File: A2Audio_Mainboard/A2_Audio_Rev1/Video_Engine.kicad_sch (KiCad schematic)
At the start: 21 parts, among them U18 LT6711A, U20 AP2112K-1.8, U22 AP2112K-1.2, Y2 27MHz

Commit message: Added footprints and a few more parts.
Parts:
- C58, C59, C60, C61, C62, C63, C72, C73, C74, C75, C76, C77, C78, C79, C80, C81: footprint (none) -> Capacitor_SMD:C_0402_1005Metric
- R26: footprint (none) -> Resistor_SMD:R_0402_1005Metric
- Y2: footprint (none) -> Crystal:Crystal_SMD_3225-4Pin_3.2x2.5mm
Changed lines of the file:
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@@
 			)
 		)
-		(property "Footprint" ""
+		(property "Footprint" "Capacitor_SMD:C_0402_1005Metric"
 			(at 198.12 114.6048 0)
 			(hide yes)
@@
 			)
 		)
-		(property "Footprint" ""
+		(property "Footprint" "Capacitor_SMD:C_0402_1005Metric"
 			(at 198.12 79.0448 0)
 			(hide yes)
@@
 			)
 		)
-		(property "Footprint" ""
+		(property "Footprint" "Capacitor_SMD:C_0402_1005Metric"
 			(at 198.12 131.1148 0)
 			(hide yes)
@@
 			)
 		)
-		(property "Footprint" ""
+		(property "Footprint" "Resistor_SMD:R_0402_1005Metric"
 			(at 77.47 114.808 90)
 			(hide yes)
@@
 			)
 		)
-		(property "Footprint" ""
+		(property "Footprint" "Crystal:Crystal_SMD_3225-4Pin_3.2x2.5mm"
 			(at 62.23 82.55 0)
 			(hide yes)
@@
 			)
 		)
-		(property "Footprint" ""
+		(property "Footprint" "Capacitor_SMD:C_0402_1005Metric"
 			(at 523.5448 66.04 0)
 			(hide yes)
@@
 			)
 		)
-		(property "Footprint" ""
+		(property "Footprint" "Capacitor_SMD:C_0402_1005Metric"
 			(at 198.12 71.4248 0)
 			(hide yes)
@@
 			)
 		)
-		(property "Footprint" ""
+		(property "Footprint" "Capacitor_SMD:C_0402_1005Metric"
 			(at 475.2848 62.23 0)
 			(hide yes)
@@
 			)
 		)
-		(property "Footprint" ""
+		(property "Footprint" "Capacitor_SMD:C_0402_1005Metric"
 			(at 198.12 104.4448 0)
 			(hide yes)
@@
 			)
 		)
-		(property "Footprint" ""
+		(property "Footprint" "Capacitor_SMD:C_0402_1005Metric"
 			(at 72.39 104.4448 0)
 			(hide yes)
@@
 			)
 		)
-		(property "Footprint" ""
+		(property "Footprint" "Capacitor_SMD:C_0402_1005Metric"
 			(at 198.12 95.5548 0)
 			(hide yes)
@@
 			)
 		)
-		(property "Footprint" ""
+		(property "Footprint" "Capacitor_SMD:C_0402_1005Metric"
 			(at 72.39 99.3648 0)
 			(hide yes)
@@
 			)
 		)
-		(property "Footprint" ""
+		(property "Footprint" "Capacitor_SMD:C_0402_1005Metric"
 			(at 198.12 87.9348 0)
 			(hide yes)
@@
 			)
 		)
-		(property "Footprint" ""
+		(property "Footprint" "Capacitor_SMD:C_0402_1005Metric"
 			(at 439.42 53.0352 0)
 			(hide yes)
@@
 			)
 		)
-		(property "Footprint" ""
+		(property "Footprint" "Capacitor_SMD:C_0402_1005Metric"
 			(at 41.6052 82.55 0)
 			(hide yes)
@@
 			)
 		)
-		(property "Footprint" ""
+		(property "Footprint" "Capacitor_SMD:C_0402_1005Metric"
 			(at 468.9348 85.09 0)
 			(hide yes)
@@
 			)
 		)
-		(property "Footprint" ""
+		(property "Footprint" "Capacitor_SMD:C_0402_1005Metric"
 			(at 27.6352 82.55 0)
 			(hide yes)
@@
 			)
 		)
-		(property "Footprint" ""
+		(property "Footprint" "Capacitor_SMD:C_0402_1005Metric"
 			(at 198.12 123.4948 0)
 			(hide yes)

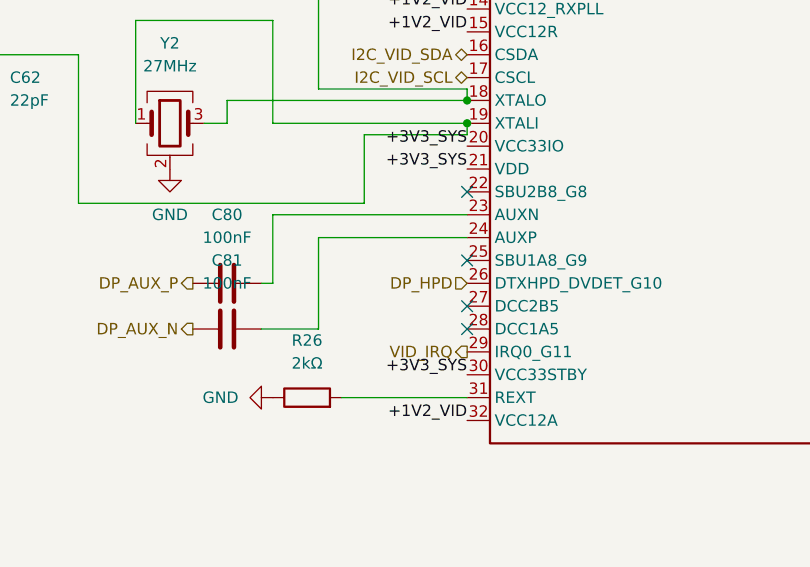
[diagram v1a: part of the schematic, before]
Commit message: Fixing ERC errors
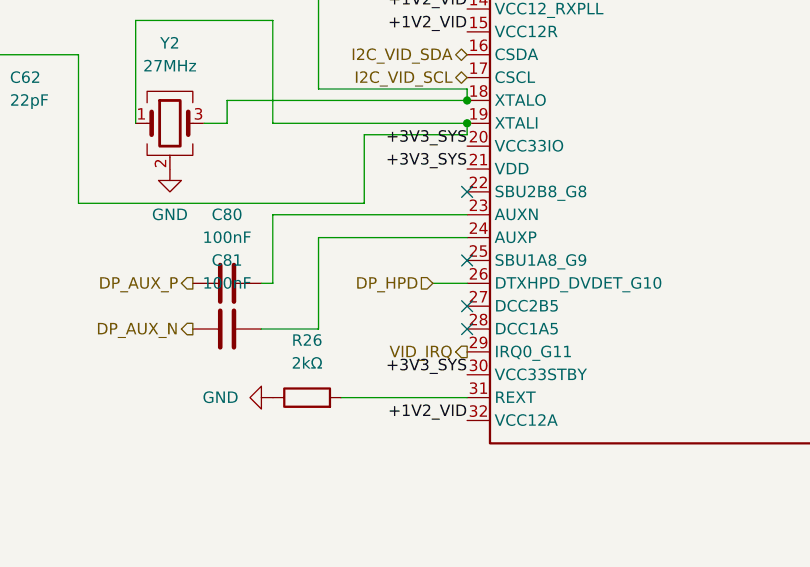
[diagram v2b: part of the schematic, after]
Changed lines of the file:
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@@
+	(wire
+		(pts
+			(xy 91.44 100.33) (xy 95.25 100.33)
+		)
+		(stroke
+			(width 0)
+			(type default)
+		)
+	)
 	(wire
 		(pts
@@
 	(hierarchical_label "DP_HPD"
 		(shape input)
-		(at 95.25 100.33 180)
-		(effects
-			(font
+		(at 91.44 100.33 180)
+		(effects
+			(font

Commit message: Fixed even more schematic errors
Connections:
- net GND: now also U20.2 (GND), U22.2 (GND)
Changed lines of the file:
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@@
+	(symbol
+		(lib_id "symbols:GND")
+		(at 454.66 73.66 0)
+		(unit 1)
+		(body_style 1)
+		(exclude_from_sim no)
+		(in_bom yes)
+		(on_board yes)
+		(in_pos_files yes)
+		(dnp no)
+		(fields_autoplaced yes)
+		(property "Reference" "#PWR091"
+			(at 454.66 80.01 0)
+			(hide yes)
+			(show_name no)
+			(do_not_autoplace no)
+			(effects
+				(font
+					(size 1.27 1.27)
+				)
+			)
+		)
+		(property "Value" "GND"
+			(at 454.66 78.74 0)
+			(show_name no)
+			(do_not_autoplace no)
+			(effects
+				(font
+					(size 1.27 1.27)
+				)
+			)
+		)
+		(property "Footprint" ""
+			(at 454.66 73.66 0)
+			(hide yes)
+			(show_name no)
+			(do_not_autoplace no)
+			(effects
+				(font
+					(size 1.27 1.27)
+				)
+			)
+		)
+		(property "Datasheet" ""
+			(at 454.66 73.66 0)
+			(hide yes)
+			(show_name no)
+			(do_not_autoplace no)
+			(effects
+				(font
+					(size 1.27 1.27)
+				)
+			)
+		)
+		(property "Description" "Power symbol creates a global label with name \"GND\" , ground"
+			(at 454.66 73.66 0)
+			(hide yes)
+			(show_name no)
+			(do_not_autoplace no)
+			(effects
+				(font
+					(size 1.27 1.27)
+				)
+			)
+		)
+		(pin "1"
+		)
+		(instances
+			(project "A2_Audio_Rev1"
+				(path "/6bc02254-56bf-4f9a-8c1a-77c700c92092/26c47db4-7e54-4843-a169-bd943818f1c9"
+					(reference "#PWR091")
+					(unit 1)
+				)
+			)
+		)
+	)
 	(symbol
 		(lib_id "symbols:GND")
@@
 					(unit 1)
 				)
+			)
+		)
+	)
+	(symbol
+		(lib_id "symbols:GND")
+		(at 509.27 76.2 0)
+		(unit 1)
+		(body_style 1)
+		(exclude_from_sim no)
+		(in_bom yes)
+		(on_board yes)
+		(in_pos_files yes)
+		(dnp no)
+		(fields_autoplaced yes)
+		(property "Reference" "#PWR092"
+			(at 509.27 82.55 0)
+			(hide yes)
+			(show_name no)
+			(do_not_autoplace no)
+			(effects
+				(font
+					(size 1.27 1.27)
+				)
+			)
+		)
+		(property "Value" "GND"
+			(at 509.27 81.28 0)
+			(show_name no)
+			(do_not_autoplace no)
+			(effects
+				(font
+					(size 1.27 1.27)
+				)
+			)
+		)
+		(property "Footprint" ""
+			(at 509.27 76.2 0)
+			(hide yes)
+			(show_name no)
+			(do_not_autoplace no)
+			(effects
+				(font
+					(size 1.27 1.27)
+				)
+			)
+		)
+		(property "Datasheet" ""
+			(at 509.27 76.2 0)
+			(hide yes)
+			(show_name no)
+			(do_not_autoplace no)
+			(effects
+				(font
+					(size 1.27 1.27)
+				)
+			)
+		)
+		(property "Description" "Power symbol creates a global label with name \"GND\" , ground"
+			(at 509.27 76.2 0)
+			(hide yes)
+			(show_name no)
+			(do_not_autoplace no)
+			(effects
+				(font
+					(size 1.27 1.27)
+				)
+			)
+		)
+		(pin "1"
+		)
+		(instances
+			(project "A2_Audio_Rev1"
+				(path "/6bc02254-56bf-4f9a-8c1a-77c700c92092/26c47db4-7e54-4843-a169-bd943818f1c9"
+					(reference "#PWR092")
+					(unit 1)
+				)

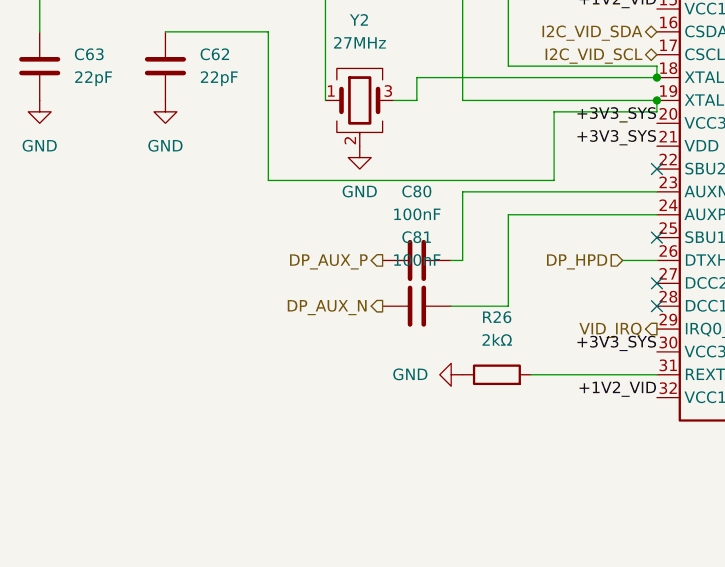
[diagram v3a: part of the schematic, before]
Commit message: Fixed SD Card logic and power error
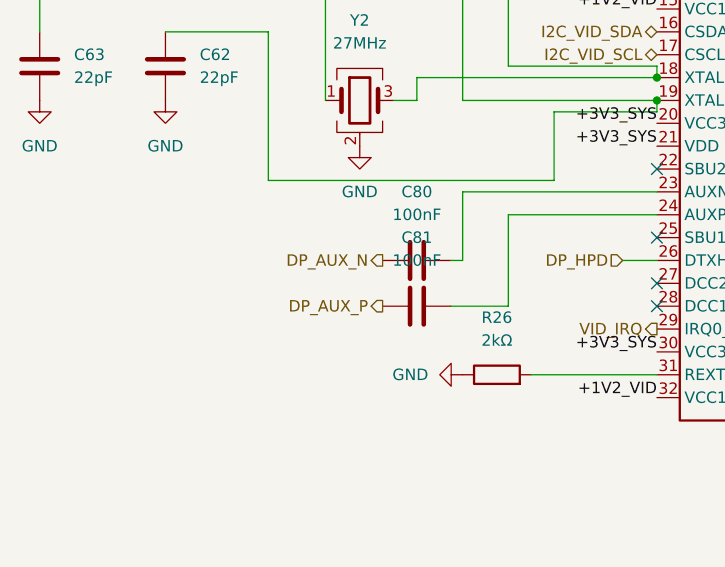
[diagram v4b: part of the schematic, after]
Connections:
- net DP_AUX_N: now also C80.1; no longer C81.1
- net DP_AUX_P: now also C81.1; no longer C80.1
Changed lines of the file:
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@@
 	(hierarchical_label "DP_AUX_N"
 		(shape output)
-		(at 64.77 105.41 180)
+		(at 64.77 100.33 180)
 		(effects
 			(font
@@
 	(hierarchical_label "DP_AUX_P"
 		(shape output)
-		(at 64.77 100.33 180)
+		(at 64.77 105.41 180)
 		(effects
 			(font
